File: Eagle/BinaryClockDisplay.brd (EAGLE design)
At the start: 75.9 x 59.7 mm, 53 parts, among them U1 DS1307Z, Y1 32.768kHz

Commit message: Started working with sw for v 2
A real state-machine and some structural changes.
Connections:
- net N$24 renamed VBATT
- net 3V3: now also JP2.17
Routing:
- net 3V3: track 114.8 -> 50.7 mm
- net GND: track 660.2 -> 617.4 mm
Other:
- board text added: "BinaryClock v. 3 Design: Pär Sundbäck"
- board text removed: "BinaryClock v. 2 Design: Pär Sundbäck"
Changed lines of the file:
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@@
 <hole x="4" y="13" drill="4"/>
 <hole x="72.8" y="12.8" drill="4"/>
-<text x="14.8" y="56.5" size="1.778" layer="26" rot="MR180">BinaryClock v. 2
+<text x="14.8" y="56.5" size="1.778" layer="26" rot="MR180">BinaryClock v. 3
 Design: Pär Sundbäck</text>
 <text x="12.9" y="62.1" size="1.778" layer="26" rot="MR0">1</text>
@@
 <text x="28" y="15.1" size="1.778" layer="26" rot="MR0">S2</text>
 <text x="38.2" y="15.2" size="1.778" layer="26" rot="MR0">S1</text>
-<text x="52.8" y="43.3" size="1.778" layer="26" rot="MR0">http://github.com/teddycool/binaryclock</text>
+<text x="49.9" y="43.1" size="1.778" layer="26" rot="MR0">http://github.com/teddycool/binaryclock</text>
 <text x="49.7" y="59.1" size="1.778" layer="26" rot="MR0">Raspberry pi IO</text>
 </plain>
@@
 <wire x1="59.809471875" y1="15.909471875" x2="69.309471875" y2="15.909471875" width="0.1524" layer="1"/>
 <wire x1="69.309471875" y1="15.909471875" x2="71.3" y2="17.9" width="0.1524" layer="1"/>
-<wire x1="71.3" y1="17.9" x2="71.3" y2="60.68" width="0.1524" layer="1"/>
 <via x="37.8" y="48.2" extent="1-16" drill="0.35"/>
 <wire x1="39.74" y1="48.26" x2="37.86" y2="48.26" width="0.1524" layer="16"/>
@@
 </polygon>
 <contactref element="JP4" pad="5"/>
-<wire x1="65.87" y1="60.68" x2="71.3" y2="60.68" width="0.1524" layer="1"/>
-<wire x1="71.3" y1="60.68" x2="73.2" y2="60.68" width="0.1524" layer="1"/>
+<wire x1="65.87" y1="60.68" x2="73.2" y2="60.68" width="0.1524" layer="1"/>
 <wire x1="63.1" y1="63.45" x2="65.87" y2="60.68" width="0.1524" layer="1"/>
 <wire x1="2.8" y1="59.47" x2="1.63" y2="58.3" width="0.2" layer="1"/>
@@
 <wire x1="40.04" y1="44.4" x2="48.081084375" y2="44.4" width="0.1524" layer="16"/>
 <wire x1="48.081084375" y1="44.4" x2="48.169709375" y2="44.4" width="0.1524" layer="16"/>
+<wire x1="62.193" y1="49.86" x2="65.87" y2="60.68" width="0" layer="19" extent="1-1"/>
 </signal>
 <signal name="N$6">
@@
 <contactref element="D3" pad="2"/>
 <contactref element="D4" pad="4"/>
-<wire x1="67.347" y1="40.97" x2="62.193" y2="46.124" width="0.1524" layer="1"/>
-<wire x1="62.193" y1="46.124" x2="62.193" y2="46.66" width="0.1524" layer="1"/>
+<wire x1="67.347" y1="40.97" x2="67.347" y2="41.506" width="0.1524" layer="1"/>
+<wire x1="67.347" y1="41.506" x2="62.193" y2="46.66" width="0.1524" layer="1"/>
 </signal>
 <signal name="GPIO18">
@@
 <wire x1="44.45" y1="52.07" x2="44.12" y2="52.4" width="0.1524" layer="1"/>
 <wire x1="44.12" y1="52.4" x2="37.5" y2="52.4" width="0.1524" layer="1"/>
-<wire x1="37.5" y1="52.4" x2="36.4" y2="51.3" width="0.1524" layer="1"/>
-<wire x1="36.4" y1="51.3" x2="36.4" y2="18.8" width="0.1524" layer="1"/>
-<wire x1="36.4" y1="18.8" x2="34.3" y2="16.7" width="0.1524" layer="1"/>
-<wire x1="34.3" y1="16.7" x2="30.6" y2="16.7" width="0.1524" layer="1"/>
+<wire x1="37.5" y1="52.4" x2="33.5" y2="48.4" width="0.1524" layer="1"/>
+<wire x1="33.5" y1="48.4" x2="33.5" y2="16.7" width="0.1524" layer="1"/>
+<wire x1="33.5" y1="16.7" x2="30.6" y2="16.7" width="0.1524" layer="1"/>
 <wire x1="30.6" y1="16.7" x2="29.21" y2="18.09" width="0.1524" layer="1"/>
 <wire x1="29.21" y1="18.09" x2="29.21" y2="19.05" width="0.1524" layer="1"/>
@@
 <wire x1="69.85" y1="44.45" x2="67.75" y2="46.55" width="0.1524" layer="1"/>
 <wire x1="67.75" y1="46.55" x2="67.64" y2="46.66" width="0.1524" layer="1"/>
-<wire x1="67.64" y1="46.66" x2="67.347" y2="46.66" width="0.1524" layer="1"/>
 <wire x1="69.85" y1="44.45" x2="69.85" y2="40.273" width="0.1524" layer="1"/>
 <wire x1="58.457" y1="37.77" x2="59.69" y2="36.537" width="0.1524" layer="1"/>
@@
 <wire x1="60.5" y1="52.9" x2="59.5" y2="51.9" width="0.1524" layer="1"/>
 <wire x1="59.5" y1="51.9" x2="59.5" y2="48.2" width="0.1524" layer="1"/>
-<wire x1="59.5" y1="48.2" x2="59.5" y2="41.5757875" width="0.1524" layer="1"/>
-<wire x1="59.5" y1="41.5757875" x2="59.5111" y2="41.5646875" width="0.1524" layer="1"/>
-<wire x1="59.5111" y1="41.5646875" x2="59.5111" y2="39.8111" width="0.1524" layer="1"/>
+<wire x1="59.5111" y1="48.2" x2="59.5111" y2="39.8111" width="0.1524" layer="1"/>
 <wire x1="59.5111" y1="39.8111" x2="58.9" y2="39.2" width="0.1524" layer="1"/>
 <wire x1="43.217" y1="46.66" x2="44.2" y2="47.643" width="0.1524" layer="1"/>
@@
 <wire x1="41.54" y1="48.26" x2="44.14" y2="48.26" width="0.1524" layer="16"/>
 <wire x1="44.14" y1="48.26" x2="44.2" y2="48.2" width="0.1524" layer="16"/>
+<wire x1="59.5111" y1="48.2" x2="59.5" y2="48.2" width="0.1524" layer="1"/>
 <wire x1="59.5" y1="48.2" x2="47.4" y2="48.2" width="0.1524" layer="1"/>
 <wire x1="47.4" y1="48.2" x2="44.2" y2="48.2" width="0.1524" layer="1"/>
@@
 <wire x1="44.2" y1="53.9" x2="44.2" y2="48.2" width="0.1524" layer="16"/>
 <wire x1="42.695" y1="55.405" x2="44.2" y2="53.9" width="0.1524" layer="16"/>
+<wire x1="67.64" y1="46.66" x2="67.347" y2="46.66" width="0" layer="19" extent="1-1"/>
 </signal>
 <signal name="3V3">
@@
 <wire x1="14.84" y1="60.069940625" x2="14.738371875" y2="59.9683125" width="0.1524" layer="16"/>
 <contactref element="JP4" pad="4"/>
-<wire x1="73.2" y1="58.14" x2="75.3" y2="60.24" width="0.1524" layer="1"/>
-<wire x1="67.6238" y1="67.6762" x2="27.3762" y2="67.6762" width="0.1524" layer="1"/>
-<wire x1="27.3762" y1="67.6762" x2="26.3" y2="66.6" width="0.1524" layer="1"/>
 <wire x1="25.7" y1="61.1" x2="16.2" y2="61.1" width="0.1524" layer="1"/>
 <wire x1="16.2" y1="61.1" x2="14.84" y2="62.46" width="0.1524" layer="1"/>
 <wire x1="14.84" y1="62.46" x2="14.84" y2="63.45" width="0.1524" layer="1"/>
-<wire x1="26.3" y1="66.6" x2="26.3" y2="61.7" width="0.1524" layer="1"/>
-<wire x1="26.3" y1="61.7" x2="25.7" y2="61.1" width="0.1524" layer="1"/>
-<wire x1="75.3" y1="60.24" x2="75.3" y2="62.2" width="0.1524" layer="1"/>
-<wire x1="75" y1="62.5" x2="75.3" y2="62.2" width="0.1524" layer="1"/>
-<wire x1="69" y1="66.3" x2="69" y2="63.5" width="0.1524" layer="1"/>
-<wire x1="69" y1="66.3" x2="67.6238" y2="67.6762" width="0.1524" layer="1"/>
-<wire x1="69" y1="63.5" x2="70" y2="62.5" width="0.1524" layer="1"/>
-<wire x1="70" y1="62.5" x2="75" y2="62.5" width="0.1524" layer="1"/>
+<contactref element="JP2" pad="17"/>
+<wire x1="35.16" y1="63.45" x2="73.2" y2="58.14" width="0" layer="19" extent="1-1"/>
+<wire x1="25.7" y1="61.1" x2="35.16" y2="63.45" width="0" layer="19" extent="1-1"/>
 </signal>
 <signal name="GPIO19">
@@
 <wire x1="47.065" y1="54.2" x2="47" y2="54.135" width="0.1524" layer="16"/>
 </signal>
-<signal name="N$24">
+<signal name="VBATT">
 <contactref element="BT1" pad="1"/>
 <contactref element="U1" pad="3"/>

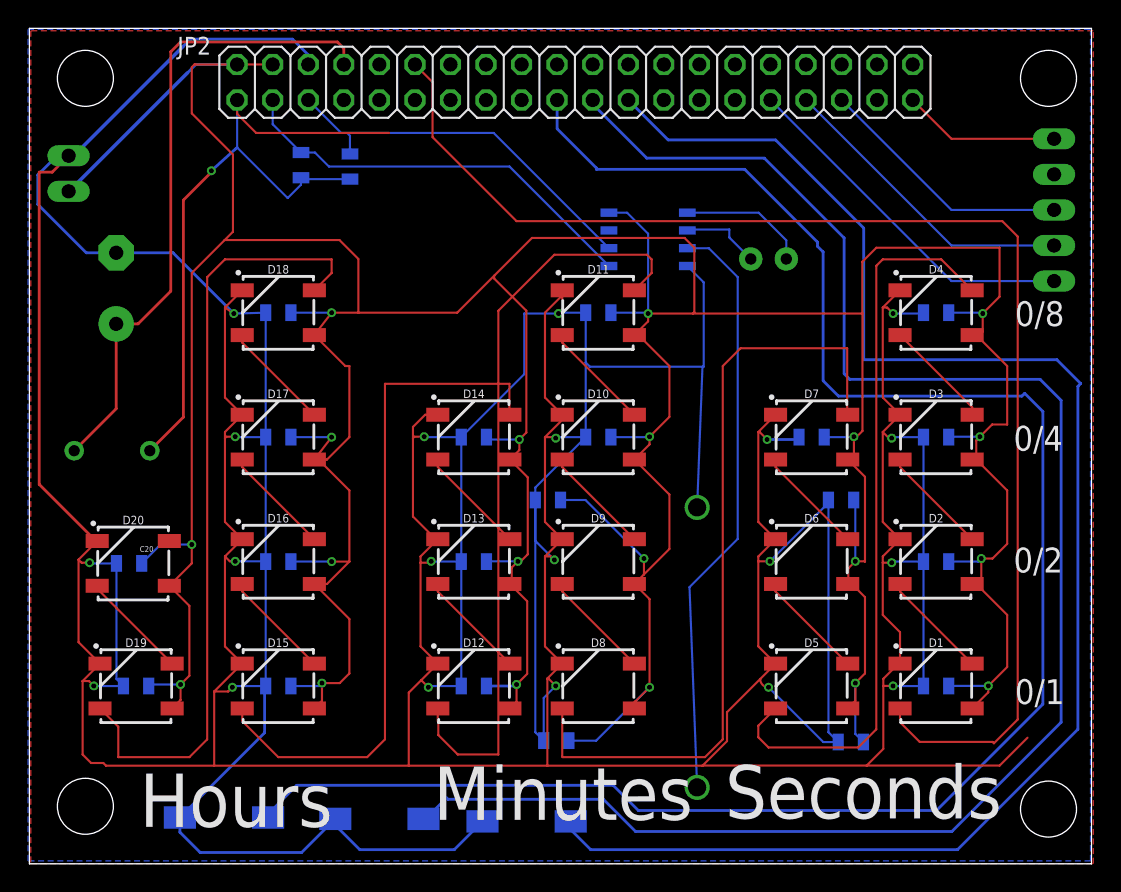
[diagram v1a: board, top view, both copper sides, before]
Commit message: HW version 4
Hardware version 4, not yet ordered. Only differnce from v 3 is the placement of the push-buttons.
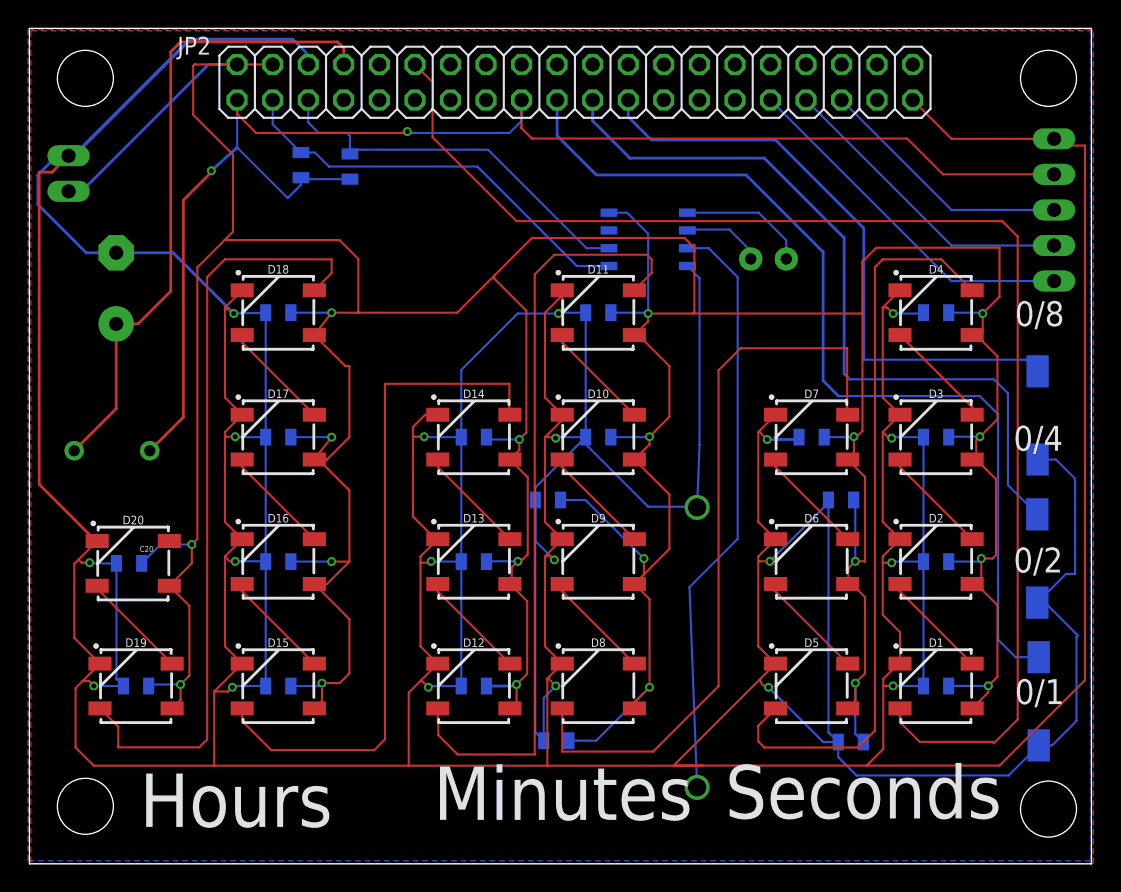
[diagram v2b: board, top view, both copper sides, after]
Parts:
- moved S3 58.8 mm to (72.1, 20.5), turned to 90 degrees
- moved S2 50.5 mm to (72.0, 30.7), turned to 90 degrees
- moved S1 46.6 mm to (72.0, 40.9), turned to 90 degrees
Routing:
- net GPIO11: track 112.0 -> 43.5 mm
- net GPIO9: track 121.6 -> 54.4 mm
- net GPIO10: track 132.1 -> 67.2 mm
- net GND: track 617.4 -> 675.0 mm
- net 3V3: track 50.7 -> 103.6 mm, vias 1 -> 2
- net N$15: track 56.3 -> 53.4 mm
- net 5V: track 405.7 -> 403.5 mm
- net N$14: track 53.9 -> 55.5 mm
- net N$26: track 56.1 -> 55.1 mm
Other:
- board text added: "BinaryClock v. 4 Design: Pär Sundbäck"
- board text removed: "BinaryClock v. 3 Design: Pär Sundbäck"
- board text removed: "S1"
- board text removed: "S2"
- board text removed: "S3"
